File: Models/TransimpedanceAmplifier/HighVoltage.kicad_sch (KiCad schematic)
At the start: 6 parts, among them U11 LM78L15, 15V, 5%, U12 LM79L15, -15V, 5%

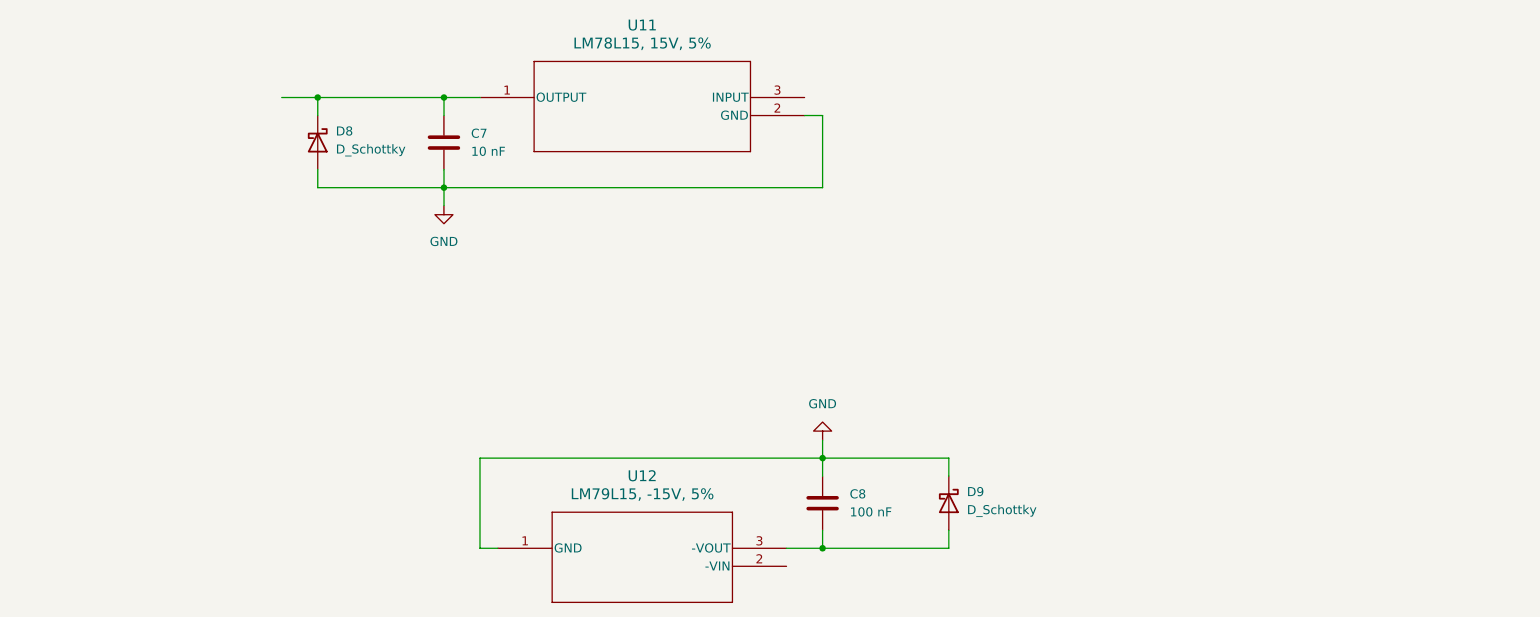
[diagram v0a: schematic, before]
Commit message: Labeled all the input/output nodes of the power subsystems
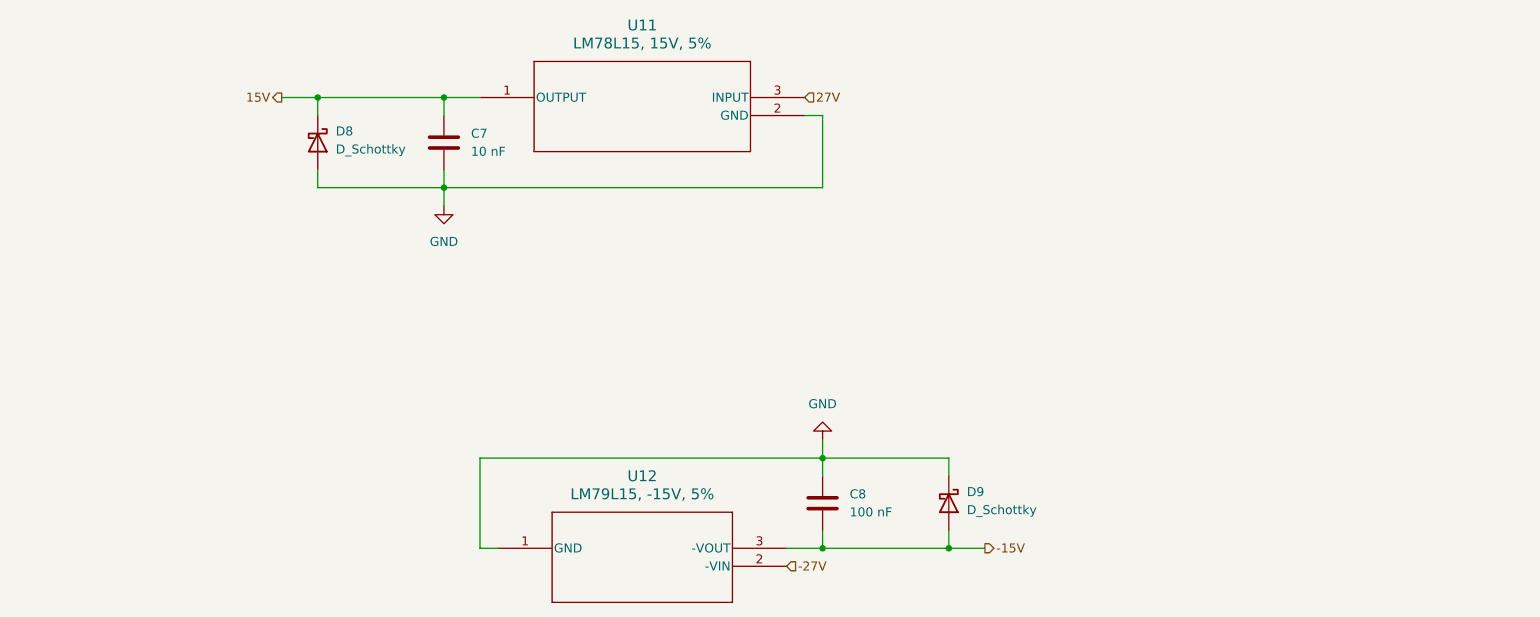
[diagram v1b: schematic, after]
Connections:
- net -15V: now reaches C8.2, D9.2 (A), U12.3 (-VOUT)
- net 15V: now reaches C7.1, D8.1 (K), U11.1 (OUTPUT)
- net 27V: now reaches U11.3 (INPUT)
- net -27V: now reaches U12.2 (-VIN)
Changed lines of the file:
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@@
+	)
+	(junction
+		(at 185.42 119.38)
+		(diameter 0)
+		(color 0 0 0 0)
 	)
 	(junction
@@
 	(wire
 		(pts
+			(xy 185.42 119.38) (xy 190.5 119.38)
+		)
+		(stroke
+			(width 0)
+			(type default)
+		)
+	)
+	(wire
+		(pts
 			(xy 96.52 66.04) (xy 96.52 68.58)
 		)
@@
 		)
 	)
+	(hierarchical_label "27V"
+		(shape input)
+		(at 165.1 55.88 0)
+		(effects
+			(font
+				(size 1.27 1.27)
+			)
+			(justify left)
+		)
+	)
+	(hierarchical_label "-15V"
+		(shape output)
+		(at 190.5 119.38 0)
+		(effects
+			(font
+				(size 1.27 1.27)
+			)
+			(justify left)
+		)
+	)
+	(hierarchical_label "15V"
+		(shape output)
+		(at 91.44 55.88 180)
+		(effects
+			(font
+				(size 1.27 1.27)
+			)
+			(justify right)
+		)
+	)
+	(hierarchical_label "-27V"
+		(shape input)
+		(at 162.56 121.92 0)
+		(effects
+			(font
+				(size 1.27 1.27)
+			)
+			(justify left)
+		)
+	)

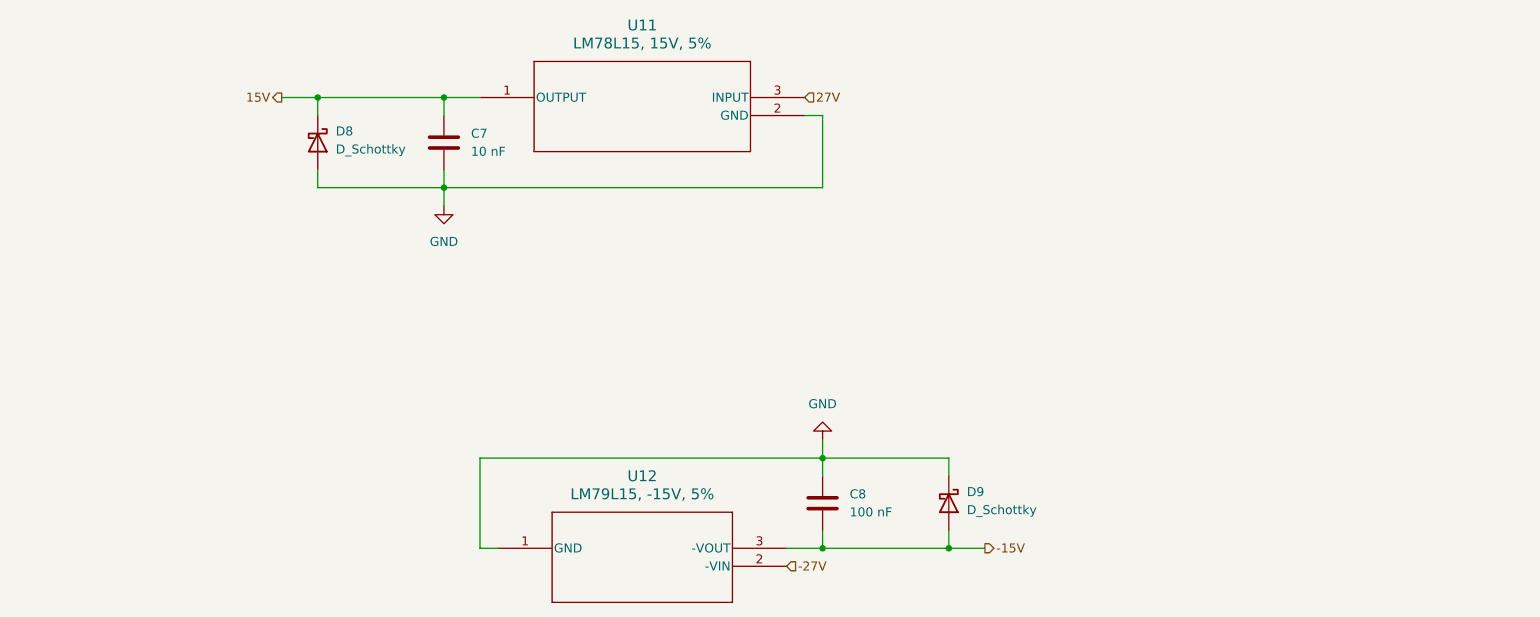
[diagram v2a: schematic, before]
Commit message: Added purchase links for all current capacitors, with dimensional tolerances matching the footprint
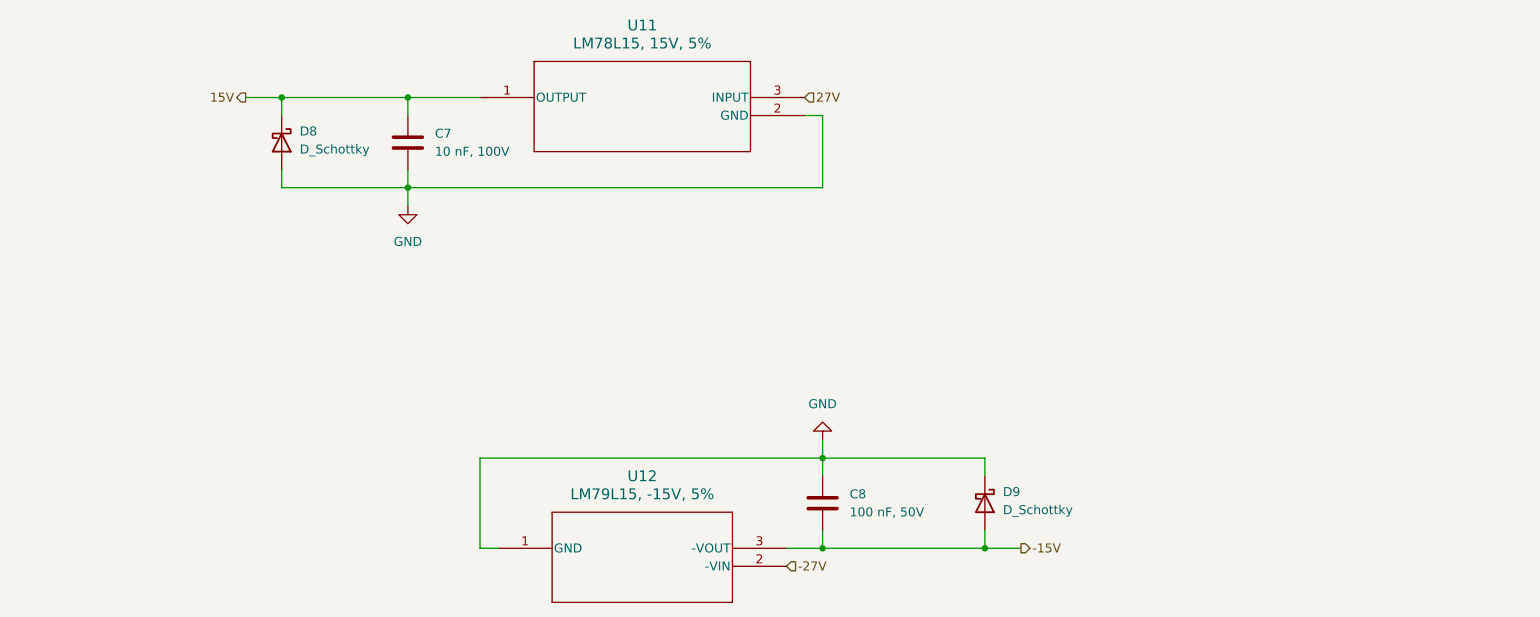
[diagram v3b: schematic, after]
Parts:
- C7: value 10 nF -> 10 nF, 100V; Purchase Link (none) -> https://www.digikey.com/en/products/detail/murata-electroni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
- C8: value 100 nF -> 100 nF, 50V; Purchase Link (none) -> https://www.digikey.com/en/products/detail/murata-electroni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
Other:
- moved on the sheet: C7, D8, D9

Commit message: All suppliers are out of stock of LM7915L in the simple TO-92-3 package. Resolve this by first tabulating the maximum possible current on each regulator.
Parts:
- U11: Purchase Link (none) -> https://www.digikey.com/en/products/detail/texas-instrument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
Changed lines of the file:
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@@
 			)
 		)
-		(property "Purchase Link" ""
+		(property "Purchase Link" "https://www.digikey.com/en/products/detail/texas-instruments/LM78L15ACZ-NOPB/6343"
 			(at 119.38 55.88 0)
 			(effects

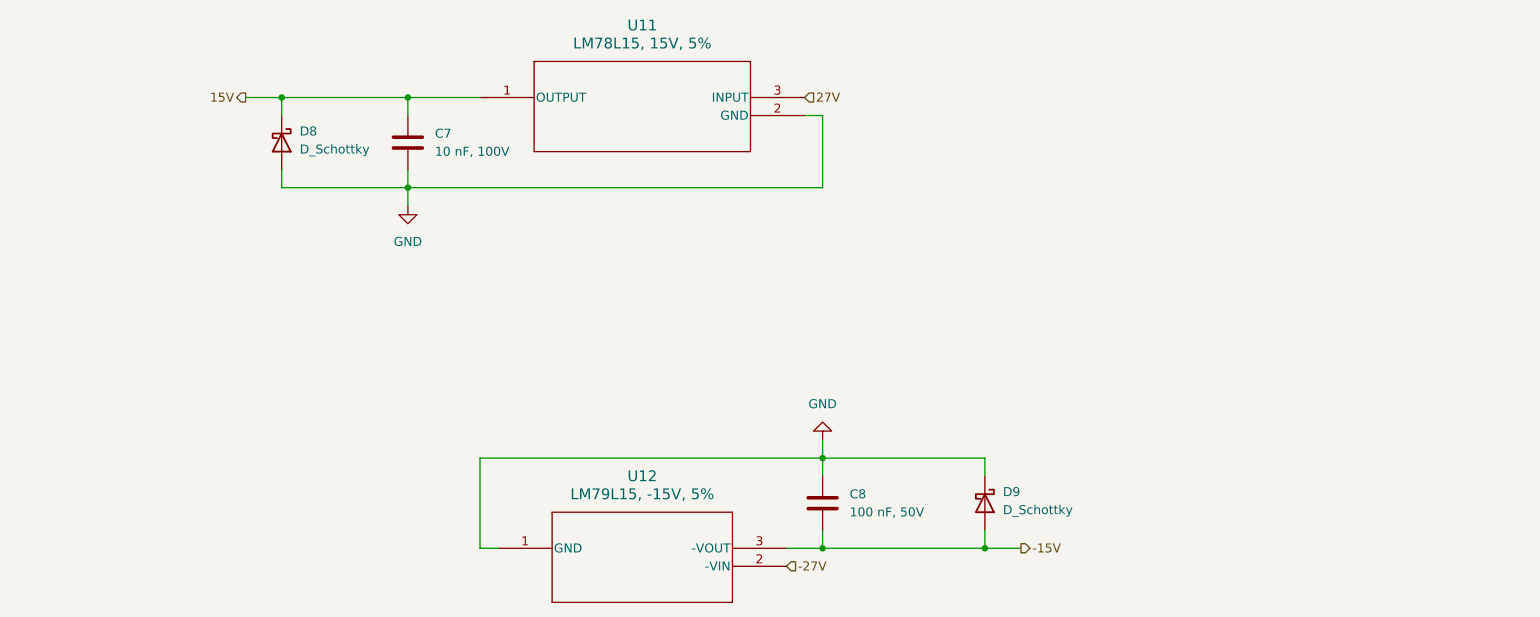
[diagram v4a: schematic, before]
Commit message: Removed all protection diodes for now
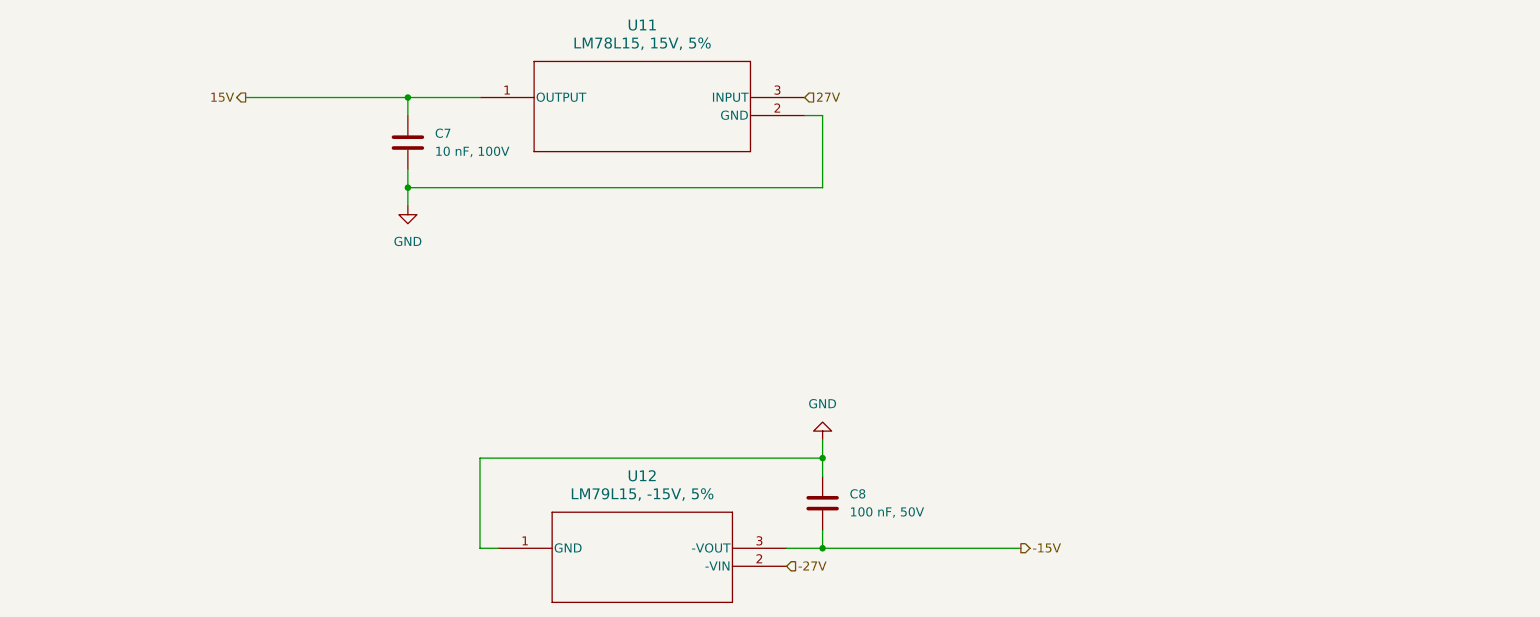
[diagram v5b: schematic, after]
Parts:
- removed D8, D9: D_Schottky, symbol Device:D_Schottky
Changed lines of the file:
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@@
-	)
-	(junction
-		(at 91.44 55.88)
-		(diameter 0)
-		(color 0 0 0 0)
-	)
-	(junction
-		(at 190.5 119.38)
-		(diameter 0)
-		(color 0 0 0 0)
 	)
 	(junction
@@
 	(wire
 		(pts
-			(xy 190.5 119.38) (xy 195.58 119.38)
-		)
-		(stroke
-			(width 0)
-			(type default)
-		)
-	)
-	(wire
-		(pts
-			(xy 91.44 66.04) (xy 91.44 68.58)
-		)
-		(stroke
-			(width 0)
-			(type default)
-		)
-	)
-	(wire
-		(pts
-			(xy 167.64 119.38) (xy 190.5 119.38)
+			(xy 167.64 119.38) (xy 195.58 119.38)
 		)
 		(stroke
@@
 	(wire
 		(pts
-			(xy 91.44 68.58) (xy 109.22 68.58)
-		)
-		(stroke
-			(width 0)
-			(type default)
-		)
-	)
-	(wire
-		(pts
 			(xy 109.22 66.04) (xy 109.22 68.58)
 		)
@@
 	(wire
 		(pts
-			(xy 190.5 116.84) (xy 190.5 119.38)
-		)
-		(stroke
-			(width 0)
-			(type default)
-		)
-	)
-	(wire
-		(pts
-			(xy 190.5 106.68) (xy 190.5 109.22)
-		)
-		(stroke
-			(width 0)
-			(type default)
-		)
-	)
-	(wire
-		(pts
-			(xy 86.36 55.88) (xy 91.44 55.88)
-		)
-		(stroke
-			(width 0)
-			(type default)
-		)
-	)
-	(wire
-		(pts
 			(xy 167.64 106.68) (xy 119.38 106.68)
 		)
@@
 	(wire
 		(pts
-			(xy 109.22 55.88) (xy 91.44 55.88)
+			(xy 86.36 55.88) (xy 109.22 55.88)
 		)
 		(stroke
@@
 		(pts
 			(xy 167.64 58.42) (xy 167.64 68.58)
-		)
-		(stroke
-			(width 0)
-			(type default)
-		)
-	)
-	(wire
-		(pts
-			(xy 167.64 106.68) (xy 190.5 106.68)
-		)
-		(stroke
-			(width 0)
-			(type default)
-		)
-	)
-	(wire
-		(pts
-			(xy 91.44 55.88) (xy 91.44 58.42)
 		)
 		(stroke
@@
 			)
 			(justify left)
-		)
-	)
-	(symbol
-		(lib_id "Device:D_Schottky")
-		(at 190.5 113.03 270)
-		(unit 1)
-		(exclude_from_sim no)
-		(in_bom yes)
-		(on_board yes)
-		(dnp no)
-		(fields_autoplaced yes)
-		(property "Reference" "D9"
-			(at 193.04 111.4424 90)
-			(effects
-				(font
-					(size 1.27 1.27)
-				)
-				(justify left)
-			)
-		)
-		(property "Value" "D_Schottky"
-			(at 193.04 113.9824 90)
-			(effects
-				(font
-					(size 1.27 1.27)
-				)
-				(justify left)
-			)
-		)
-		(property "Footprint" ""
-			(at 190.5 113.03 0)
-			(effects
-				(font
-					(size 1.27 1.27)
-				)
-				(hide yes)
-			)
-		)
-		(property "Datasheet" "~"
-			(at 190.5 113.03 0)
-			(effects
-				(font
-					(size 1.27 1.27)
-				)
-				(hide yes)
-			)
-		)
-		(property "Description" "Schottky diode"
-			(at 190.5 113.03 0)
-			(effects
-				(font
-					(size 1.27 1.27)
-				)
-				(hide yes)
-			)
-		)
-		(pin "2"
-		)
-		(pin "1"
-		)
-		(instances
-			(project "TransimpedanceAmplifier"
-				(path "/ec9f2ae3-e40d-40eb-9760-2b611ee8efd1/d0ece2d4-5b22-4822-ad0c-e2361683ec3d/79f44061-ff24-463c-a518-31179173364f"
-					(reference "D9")
-					(unit 1)
-				)
-			)
 		)
 	)
@@
 					(unit 1)
 				)
-			)
-		)
-	)
-	(symbol
-		(lib_id "Device:D_Schottky")
-		(at 91.44 62.23 270)
-		(unit 1)
-		(exclude_from_sim no)
-		(in_bom yes)
-		(on_board yes)
-		(dnp no)
-		(fields_autoplaced yes)
-		(property "Reference" "D8"
-			(at 93.98 60.6424 90)
-			(effects
-				(font
-					(size 1.27 1.27)
-				)
-				(justify left)
-			)
-		)
-		(property "Value" "D_Schottky"
-			(at 93.98 63.1824 90)
-			(effects
-				(font
-					(size 1.27 1.27)
-				)
-				(justify left)
-			)
-		)
-		(property "Footprint" ""
-			(at 91.44 62.23 0)
-			(effects
-				(font
-					(size 1.27 1.27)
-				)
-				(hide yes)
-			)
-		)
-		(property "Datasheet" "~"
-			(at 91.44 62.23 0)
-			(effects
-				(font
-					(size 1.27 1.27)
-				)
-				(hide yes)
-			)
-		)
-		(property "Description" "Schottky diode"
-			(at 91.44 62.23 0)
-			(effects
-				(font
-					(size 1.27 1.27)
-				)
-				(hide yes)
-			)
-		)
-		(pin "1"
-		)
-		(pin "2"
-		)
-		(instances
-			(project "TransimpedanceAmplifier"
-				(path "/ec9f2ae3-e40d-40eb-9760-2b611ee8efd1/d0ece2d4-5b22-4822-ad0c-e2361683ec3d/79f44061-ff24-463c-a518-31179173364f"
-					(reference "D8")
-					(unit 1)
-				)

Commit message: Deleted all schematics for voltage regulators
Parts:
- removed C7: 10 nF, 100V, symbol Device:C
- removed C8: 100 nF, 50V, symbol Device:C
- removed U11: LM78L15, 15V, 5%, LP3_TEX, symbol LM78L:LM78L05ACZ_LFT1
- removed U12: LM79L15, -15V, 5%, LP3_TEX, symbol LM79L:LM79L05ACZ_LFT1

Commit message: Finished rewriting the schematic, just need purchase links for the new regulators
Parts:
- added C7: 1 uF, 50V, symbol Device:C
- added U11: LM7815, 15V, 5%, NDE3_TEX, symbol LM78:LM7805CT_NOPB
- added U12: LM7915, -15V, 5%, T03B_TEX, symbol LM79:LM7905CT
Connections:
- new net -15V: C7.1, U12.3 (OUT)
- new net -27V: U12.2 (IN)
- new net 15V: U11.3 (OUTPUT)
- new net 27V: U11.1 (INPUT)
- new net GND: C7.2, U11.2 (GND), U12.1 (GND)

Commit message: Overhauled the purchase links for regulators and trimpots
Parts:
- U11, U12: Purchase Link (none) -> https://www.digikey.com/en/products/detail/texas-instrument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
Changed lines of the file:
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@@
+			)
+		)
+		(property "Purchase Link" "https://www.digikey.com/en/products/detail/texas-instruments/LM7815CT-NOPB/3901976"
+			(at 59.69 81.28 0)
+			(effects
+				(font
+					(size 1.27 1.27)
+				)
+				(hide yes)
 			)
 		)
@@
 			(at 180.34 81.28 0)
 			(effects
+				(font
+					(size 1.27 1.27)
+				)
+				(hide yes)
+			)
+		)
+		(property "Purchase Link" "https://www.digikey.com/en/products/detail/texas-instruments/LM7915CT-NOPB/6357"
+			(at 180.34 81.28 0)
+			(effects
